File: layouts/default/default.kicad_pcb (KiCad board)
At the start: 2 copper layers, 9 parts

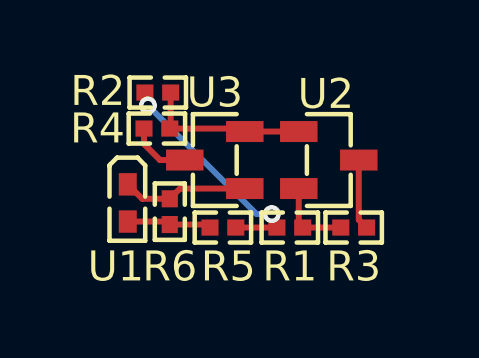
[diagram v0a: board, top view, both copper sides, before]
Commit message: better docs, removed LED
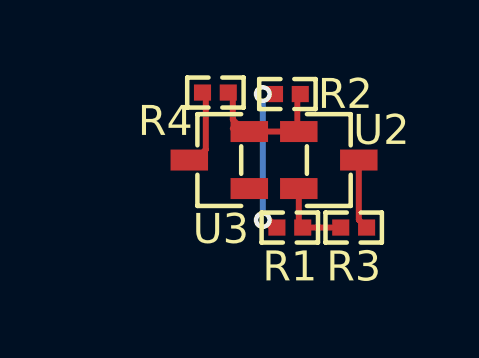
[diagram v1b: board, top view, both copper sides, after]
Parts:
- removed R5, R6: 10kΩ ±1% 62.5mW, atopile:R0402-56259e
- removed U1: , atopile:LED0402-R-RD-049f90
- moved R2 4.32 mm to (139.6, 33.4)
- moved R4 2.29 mm to (137.2, 33.3)
- moved U3 0.15 mm to (137.3, 35.5)
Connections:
- net K renamed REF-1
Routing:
- net OUT: track 4.24 -> 0.00 mm
- net anode: track 2.82 -> 0.00 mm
- net hv: track 7.80 -> 5.67 mm
- net gnd: track 2.10 -> 2.79 mm
- net REF-1: track 5.55 -> 5.04 mm
